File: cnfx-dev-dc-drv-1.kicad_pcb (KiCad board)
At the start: 2 copper layers, 51.3 x 51.3 mm, 67 parts, among them J1 Conn_01x03, J2 TC2030, J3 Conn_01x02, J4 Conn_01x02, J6 Conn_01x04_Pin, J7 Conn_01x02, J8 Conn_01x02, SW1 SW_Push, SW2 SW_Push, SW3 SW_Push, U1 SN65HVD230, U2 TPS259472A, U3 HT753-1, U4 STM32F103C8Tx, U5 DRV8837, U6 DRV8837, Y1 8M

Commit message: pcb: final layout
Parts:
- moved JP1 7.84 mm to (132.5, 80.5), turned to 0 degrees
- moved R1 6.49 mm to (139.2, 83.0), turned to 180 degrees
- moved D5 4.43 mm to (105.5, 59.5), turned to -90 degrees
- moved D7 3.59 mm to (114.0, 59.7), turned to -90 degrees
- moved C19 2.52 mm to (126.3, 91.5)
- moved C20 2.52 mm to (125.0, 93.8)
- moved C21 2.52 mm to (125.0, 95.0)
- moved U5 2.52 mm to (127.8, 93.8)
- moved TP4 2.49 mm to (129.3, 88.4)
- moved TP5 2.49 mm to (126.0, 88.4)
- moved J3 2.20 mm to (138.1, 77.1), turned to 0 degrees
- moved J4 2.03 mm to (138.1, 69.5), turned to 0 degrees
- moved SW2 1.77 mm to (136.0, 90.5)
- moved J7 1.22 mm to (127.9, 100.0)
- moved J8 1.14 mm to (117.7, 100.0)
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
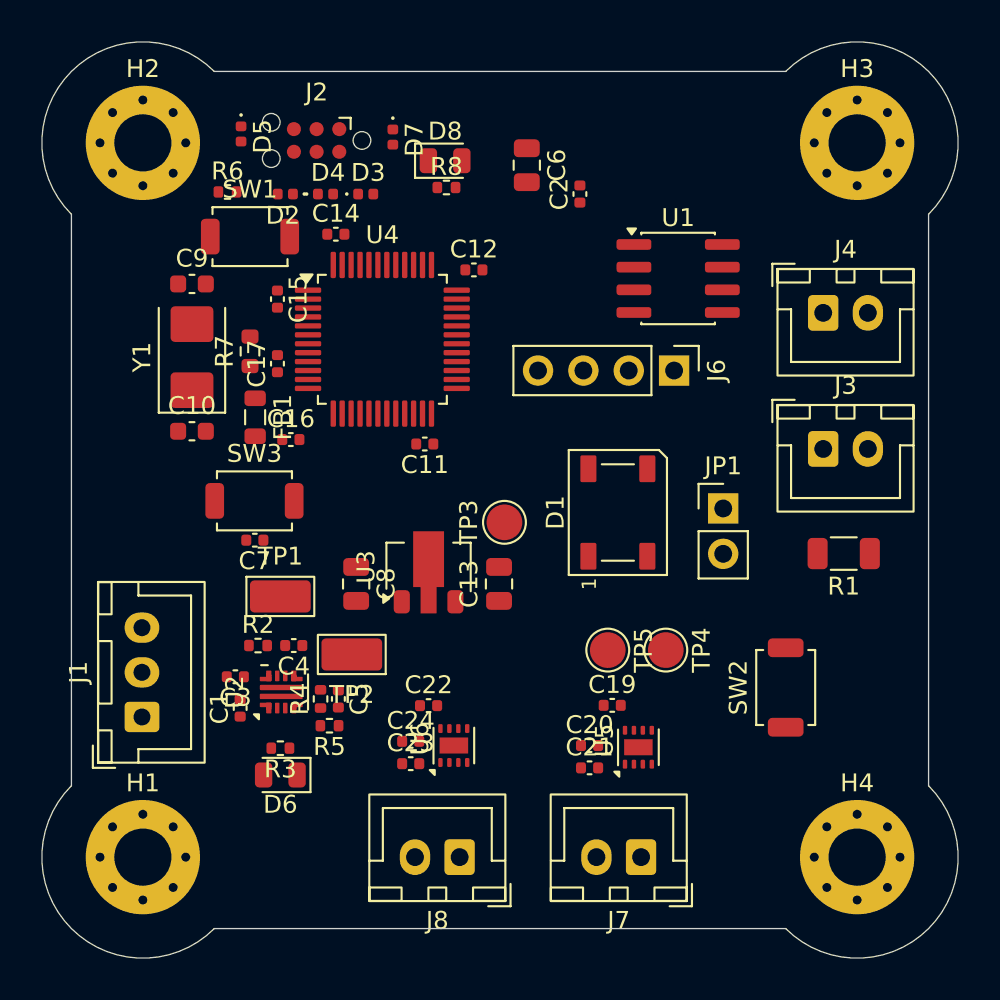
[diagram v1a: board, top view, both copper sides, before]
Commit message: pcb: add gnd vias
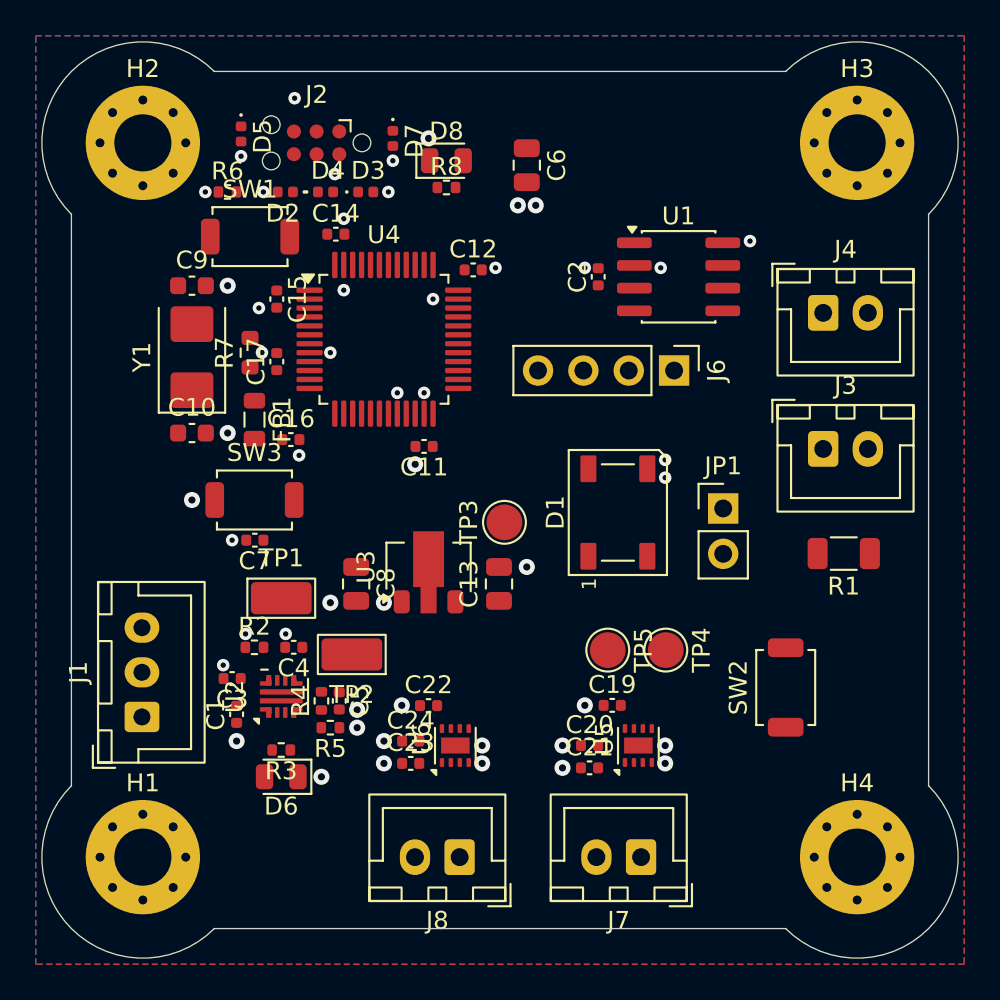
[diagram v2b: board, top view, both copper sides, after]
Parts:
- moved C2 4.75 mm to (125.5, 67.5)
- moved C1 0.40 mm to (105.2, 92.0)
- moved U2 0.25 mm to (107.8, 91.0)
- moved R2 0.22 mm to (106.2, 88.2)
- moved C3 0.21 mm to (105.0, 90.0)
- moved C11 0.14 mm to (115.8, 77.0)
- moved FB1 0.14 mm to (106.2, 75.5)
- moved J2 0.13 mm to (109.7, 60.0)
- moved C17 0.12 mm to (107.5, 72.2)
- moved C5 0.12 mm to (111.0, 91.2)
- moved R4 0.12 mm to (110.0, 91.2)
- moved R5 0.12 mm to (110.5, 92.8)
- moved D2 0.12 mm to (108.0, 62.8)
- moved D3 0.12 mm to (112.5, 62.8)
- moved D4 0.12 mm to (110.2, 62.8)
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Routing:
- net GND: vias 0 -> 50
- added copper zone on B.Cu, net GND
- added copper zone on F.Cu, net GND

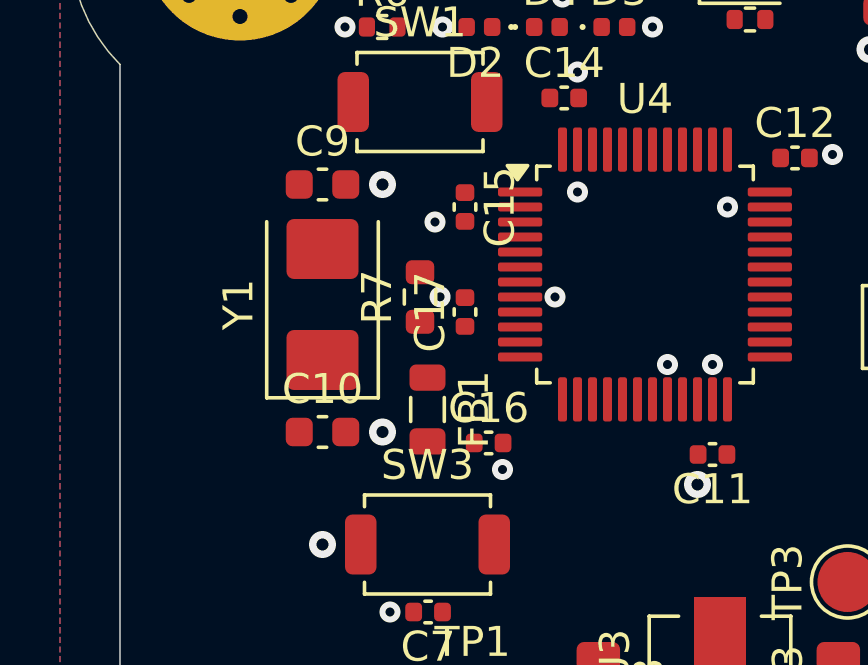
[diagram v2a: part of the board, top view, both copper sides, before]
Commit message: pcb: add XTAL routing
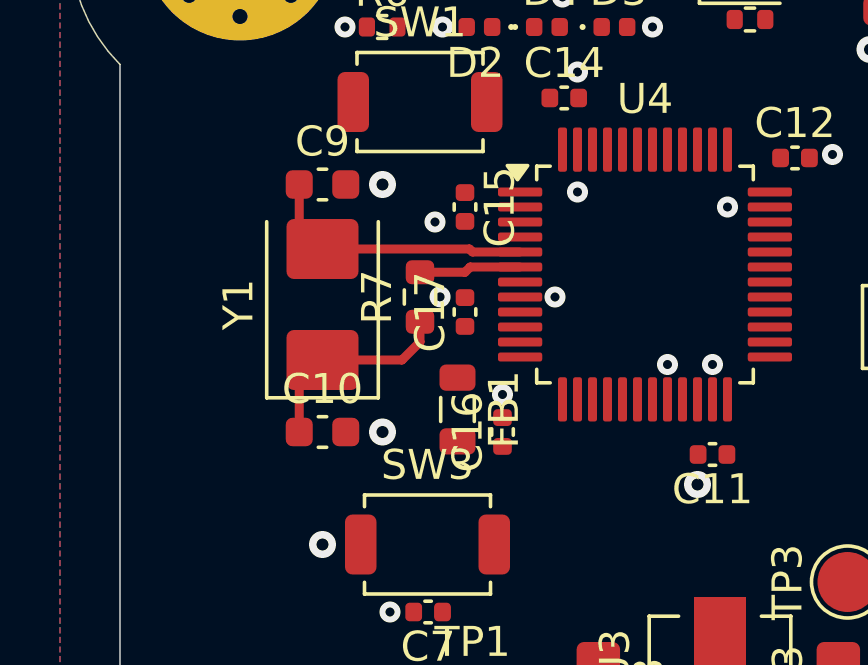
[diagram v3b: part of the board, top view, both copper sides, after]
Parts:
- moved FB1 1.00 mm to (107.2, 75.5)
- moved C16 0.59 mm to (108.8, 76.2), turned to 90 degrees
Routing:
- net /XTAL_I: track 0.00 -> 9.10 mm
- net /XTAL_RO: track 0.00 -> 6.89 mm
- net /XTAL_O: track 0.00 -> 3.41 mm
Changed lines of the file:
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@@
 	(footprint "Capacitor_SMD:C_0402_1005Metric"
 		(layer "F.Cu")
-		(at 108.2875 76.615)
+		(at 108.75 76.25 90)
 		(descr "Capacitor SMD 0402 (1005 Metric), square (rectangular) end terminal, IPC-7351 nominal, (Body size source: IPC-SM-782 page 76, https://www.pcb-3d.com/wordpress/wp-content/uploads/ipc-sm-782a_amendment_1_and_2.pdf)")
 		(tags "capacitor")
 		(property "Reference" "C16"
-			(at 0 -1.16 0)
+			(at 0 -1.16 90)
 			(layer "F.SilkS")
 			(effects
@@
 		)
 		(property "Value" "1u"
-			(at 0 1.16 0)
+			(at 0 1.16 90)
 			(layer "F.Fab")
 			(effects
@@
 		)
 		(property "Datasheet" ""
-			(at 0 0 0)
+			(at 0 0 90)
 			(layer "F.Fab")
 			(hide yes)
@@
 		)
 		(property "Description" "Unpolarized capacitor"
-			(at 0 0 0)
+			(at 0 0 90)
 			(layer "F.Fab")
 			(hide yes)
@@
 		)
 		(property "KiLib_Generator" "SMD_2terminal_chip_molded"
-			(at 0 0 0)
+			(at 0 0 90)
 			(layer "F.SilkS")
 			(hide yes)
@@
 		)
 		(property "Basic" "Y"
-			(at 0 0 0)
+			(at 0 0 90)
 			(unlocked yes)
 			(layer "F.Fab")
@@
 		)
 		(property "JLCPCB Part #" "C52923"
-			(at 0 0 0)
+			(at 0 0 90)
 			(unlocked yes)
 			(layer "F.Fab")
@@
 		)
 		(property "Manufacturer" "Samsung Electro-Mechanics "
-			(at 0 0 0)
+			(at 0 0 90)
 			(unlocked yes)
 			(layer "F.Fab")
@@
 		)
 		(property "Manufacturer Part Number" "CL05A105KA5NQNC"
-			(at 0 0 0)
+			(at 0 0 90)
 			(unlocked yes)
 			(layer "F.Fab")
@@
 		)
 		(fp_text user "${REFERENCE}"
-			(at 0 0 0)
+			(at 0 0 90)
 			(layer "F.Fab")
 			(effects
@@
 		)
 		(pad "1" smd roundrect
-			(at -0.48 0)
+			(at -0.48 0 90)
 			(size 0.56 0.62)
 			(layers "F.Cu" "F.Mask" "F.Paste")
@@
 		)
 		(pad "2" smd roundrect
-			(at 0.48 0)
+			(at 0.48 0 90)
 			(size 0.56 0.62)
 			(layers "F.Cu" "F.Mask" "F.Paste")
@@
 	(footprint "Inductor_SMD:L_0805_2012Metric"
 		(layer "F.Cu")
-		(at 106.25 75.5 -90)
+		(at 107.25 75.5 -90)
 		(descr "Inductor SMD 0805 (2012 Metric), square (rectangular) end terminal, IPC-7351 nominal, (Body size source: IPC-SM-782 page 80, https://www.pcb-3d.com/wordpress/wp-content/uploads/ipc-sm-782a_amendment_1_and_2.pdf)")
 		(tags "inductor")
@@
 	)
 	(via
-		(at 108.75 77.5)
-		(size 0.7)
-		(drill 0.3)
-		(layers "F.Cu" "B.Cu")
-		(free yes)
-		(net "GND")
-	)
-	(via
 		(at 119 93.75)
 		(size 0.9)
@@
 	)
 	(via
+		(at 108.75 75)
+		(size 0.7)
+		(drill 0.3)
+		(layers "F.Cu" "B.Cu")
+		(free yes)
+		(net "GND")
+	)
+	(via
 		(at 129.25 78.75)
 		(size 0.7)
@@
 		(net "GND")
 	)
+	(segment
+		(start 101.975 69.375)
+		(end 102.75 70.15)
+		(width 0.3)
+		(layer "F.Cu")
+		(net "/XTAL_I")
+	)
+	(segment
+		(start 101.975 68)
+		(end 101.975 69.375)
+		(width 0.3)
+		(layer "F.Cu")
+		(net "/XTAL_I")
+	)
+	(segment
+		(start 107.65 70.15)
+		(end 107.75 70.25)
+		(width 0.3)
+		(layer "F.Cu")
+		(net "/XTAL_I")
+	)
+	(segment
+		(start 107.75 70.25)
+		(end 109.3375 70.25)
+		(width 0.3)
+		(layer "F.Cu")
+		(net "/XTAL_I")
+	)
+	(segment
+		(start 102.75 70.15)
+		(end 107.65 70.15)
+		(width 0.3)
+		(layer "F.Cu")
+		(net "/XTAL_I")
+	)
+	(segment
+		(start 101.975 74.625)
+		(end 102.75 73.85)
+		(width 0.3)
+		(layer "F.Cu")
+		(net "/XTAL_RO")
+	)
+	(segment
+		(start 106 73.25)
+		(end 105.4 73.85)
+		(width 0.3)
+		(layer "F.Cu")
+		(net "/XTAL_RO")
+	)
+	(segment
+		(start 105.4 73.85)
+		(end 102.75 73.85)
+		(width 0.3)
+		(layer "F.Cu")
+		(net "/XTAL_RO")
+	)
+	(segment
+		(start 101.975 76.25)
+		(end 101.975 74.625)
+		(width 0.3)
+		(layer "F.Cu")
+		(net "/XTAL_RO")
+	)
+	(segment
+		(start 106 72.575)
+		(end 106 73.25)
+		(width 0.3)
+		(layer "F.Cu")
+		(net "/XTAL_RO")
+	)
+	(segment
+		(start 106 70.925)
+		(end 107.5 70.925)
+		(width 0.3)
+		(layer "F.Cu")
+		(net "/XTAL_O")
+	)
+	(segment
+		(start 109.3375 70.75)
+		(end 107.675 70.75)
+		(width 0.3)
+		(layer "F.Cu")
+		(net "/XTAL_O")
+	)
+	(segment
+		(start 107.675 70.75)
+		(end 107.5 70.925)
+		(width 0.3)
+		(layer "F.Cu")
+		(net "/XTAL_O")
+	)
 	(zone

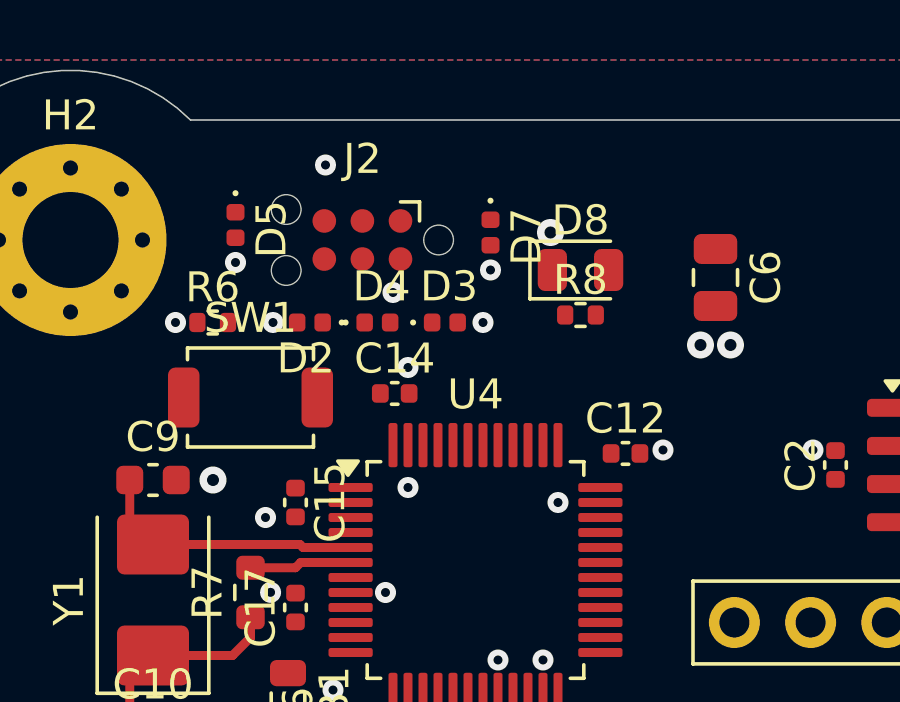
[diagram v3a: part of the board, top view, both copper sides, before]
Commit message: pcb: add SWD routing
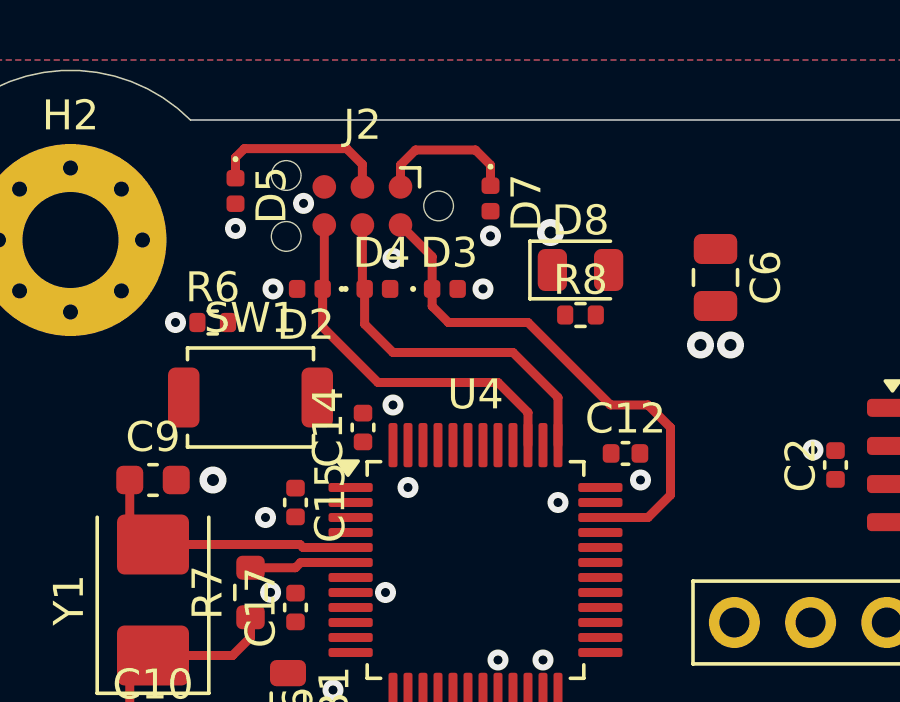
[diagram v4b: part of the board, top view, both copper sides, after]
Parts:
- moved C14 1.55 mm to (109.8, 66.2), turned to 90 degrees
- moved D5 1.13 mm to (105.5, 58.4)
- moved D7 1.13 mm to (114.0, 58.6)
- moved J2 1.13 mm to (109.7, 58.9)
- moved D2 1.12 mm to (108.0, 61.6)
- moved D3 1.12 mm to (112.5, 61.6)
- moved D4 1.12 mm to (110.2, 61.6)
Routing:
- net /SWDIO: track 0.00 -> 17.7 mm
- net /SWO: track 0.00 -> 12.5 mm
- net /SWCLK: track 0.00 -> 12.4 mm
- net /NRST: track 0.00 -> 6.01 mm
- net +3V3: track 0.00 -> 4.83 mm

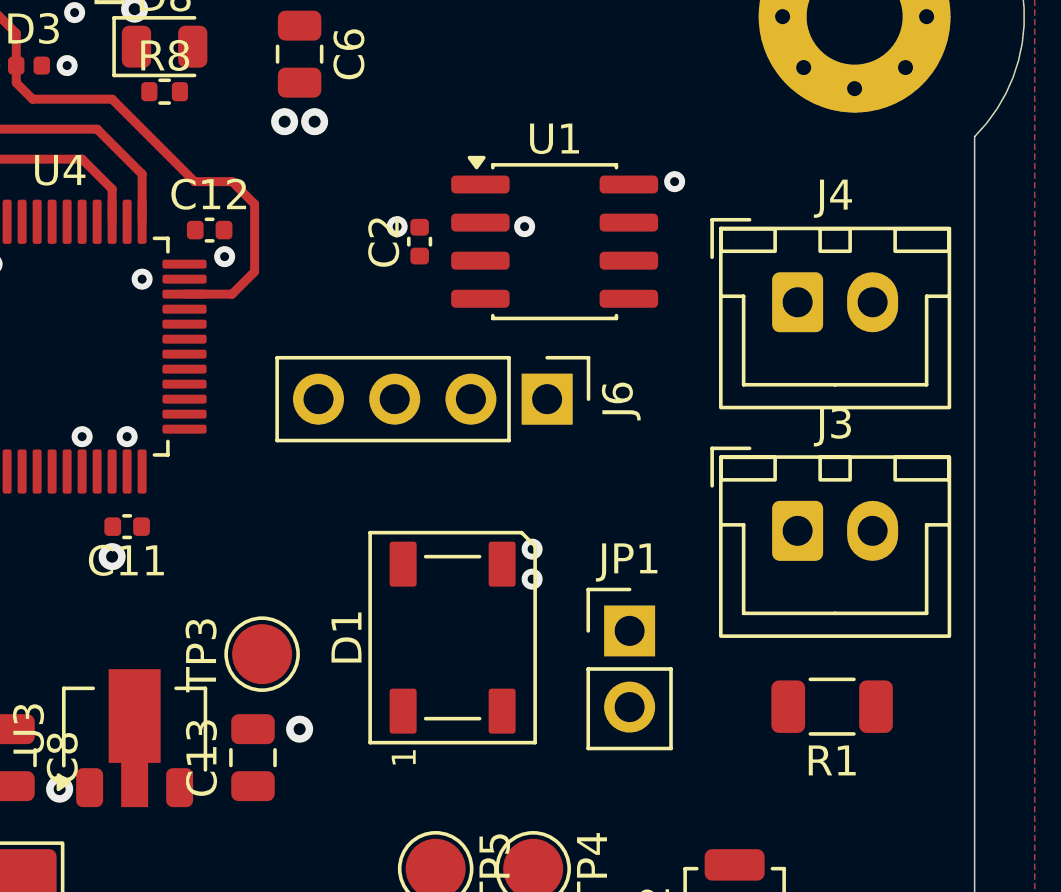
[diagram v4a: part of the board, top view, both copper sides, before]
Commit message: pcb: add can routing
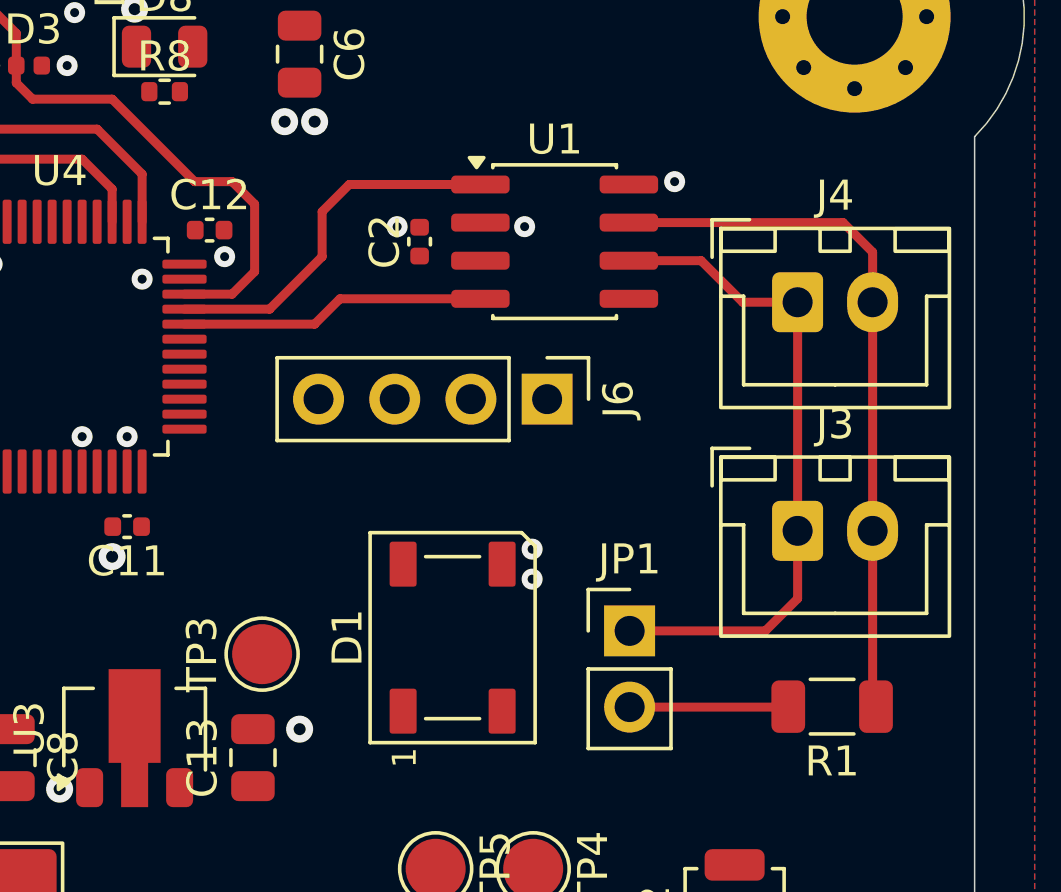
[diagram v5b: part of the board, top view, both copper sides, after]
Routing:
- net /CANH: track 0.00 -> 23.7 mm
- net /CANL: track 0.00 -> 22.1 mm
- net /CAN_TX: track 0.00 -> 12.5 mm
- net /CAN_RX: track 0.00 -> 10.2 mm
- net Net-(JP1-B): track 0.00 -> 5.29 mm
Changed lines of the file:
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@@
+	)
+	(segment
+		(start 140.6 69.52)
+		(end 140.6 77.14)
+		(width 0.3)
+		(layer "F.Cu")
+		(net "/CANH")
+	)
+	(segment
+		(start 140.6 67.85)
+		(end 140.6 69.52)
+		(width 0.3)
+		(layer "F.Cu")
+		(net "/CANH")
+	)
+	(segment
+		(start 132.475 66.865)
+		(end 139.615 66.865)
+		(width 0.3)
+		(layer "F.Cu")
+		(net "/CANH")
+	)
+	(segment
+		(start 140.6 77.14)
+		(end 140.6 82.8875)
+		(width 0.3)
+		(layer "F.Cu")
+		(net "/CANH")
+	)
+	(segment
+		(start 140.6 82.8875)
+		(end 140.7125 83)
+		(width 0.3)
+		(layer "F.Cu")
+		(net "/CANH")
+	)
+	(segment
+		(start 139.615 66.865)
+		(end 140.6 67.85)
+		(width 0.3)
+		(layer "F.Cu")
+		(net "/CANH")
+	)
+	(segment
+		(start 138.1 77.14)
+		(end 138.1 69.52)
+		(width 0.3)
+		(layer "F.Cu")
+		(net "/CANL")
+	)
+	(segment
+		(start 138.1 79.4)
+		(end 137.025 80.475)
+		(width 0.3)
+		(layer "F.Cu")
+		(net "/CANL")
+	)
+	(segment
+		(start 138.1 77.14)
+		(end 138.1 79.4)
+		(width 0.3)
+		(layer "F.Cu")
+		(net "/CANL")
+	)
+	(segment
+		(start 137.025 80.475)
+		(end 132.5 80.475)
+		(width 0.3)
+		(layer "F.Cu")
+		(net "/CANL")
+	)
+	(segment
+		(start 138.1 69.52)
+		(end 136.27 69.52)
+		(width 0.3)
+		(layer "F.Cu")
+		(net "/CANL")
+	)
+	(segment
+		(start 134.885 68.135)
+		(end 132.475 68.135)
+		(width 0.3)
+		(layer "F.Cu")
+		(net "/CANL")
+	)
+	(segment
+		(start 136.27 69.52)
+		(end 134.885 68.135)
+		(width 0.3)
+		(layer "F.Cu")
+		(net "/CANL")
+	)
+	(segment
+		(start 137.7725 83.015)
+		(end 137.7875 83)
+		(width 0.3)
+		(layer "F.Cu")
+		(net "Net-(JP1-B)")
+	)
+	(segment
+		(start 132.5 83.015)
+		(end 137.7725 83.015)
+		(width 0.3)
+		(layer "F.Cu")
+		(net "Net-(JP1-B)")
 	)
 	(segment
@@
 		(net "/XTAL_O")
 	)
+	(segment
+		(start 122.25 66.5)
+		(end 123.155 65.595)
+		(width 0.3)
+		(layer "F.Cu")
+		(net "/CAN_TX")
+	)
+	(segment
+		(start 120.5 69.75)
+		(end 122.25 68)
+		(width 0.3)
+		(layer "F.Cu")
+		(net "/CAN_TX")
+	)
+	(segment
+		(start 122.25 68)
+		(end 122.25 66.5)
+		(width 0.3)
+		(layer "F.Cu")
+		(net "/CAN_TX")
+	)
+	(segment
+		(start 117.6625 69.75)
+		(end 120.5 69.75)
+		(width 0.3)
+		(layer "F.Cu")
+		(net "/CAN_TX")
+	)
+	(segment
+		(start 123.155 65.595)
+		(end 127.525 65.595)
+		(width 0.3)
+		(layer "F.Cu")
+		(net "/CAN_TX")
+	)
+	(segment
+		(start 122.845 69.405)
+		(end 122 70.25)
+		(width 0.3)
+		(layer "F.Cu")
+		(net "/CAN_RX")
+	)
+	(segment
+		(start 122 70.25)
+		(end 117.6625 70.25)
+		(width 0.3)
+		(layer "F.Cu")
+		(net "/CAN_RX")
+	)
+	(segment
+		(start 127.525 69.405)
+		(end 122.845 69.405)
+		(width 0.3)
+		(layer "F.Cu")
+		(net "/CAN_RX")
+	)
 	(zone
